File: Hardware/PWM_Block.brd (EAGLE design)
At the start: 30.5 x 53.3 mm, 51 parts, among them U1 PCA9685, U2 PCA9306, U3 EDISON_CONNECTOR_FULLMOUNTING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, U4 EDISON_CONNECTOR_FULLHEADER

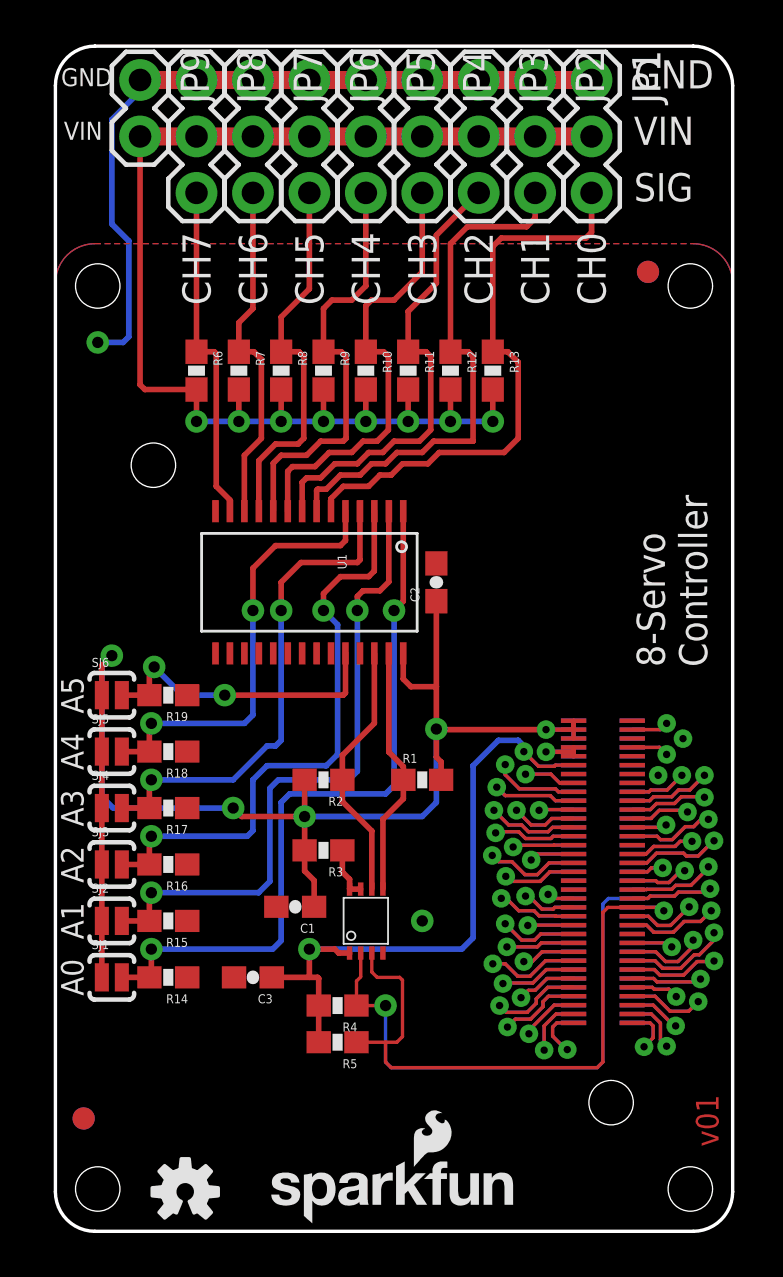
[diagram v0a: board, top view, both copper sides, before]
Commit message: Added DCIN pin Corrected Header footprint Renamed board and files Cleaned up dimensions and added units Added VSYS -> VIN circuit Added DNP to pullup resistors
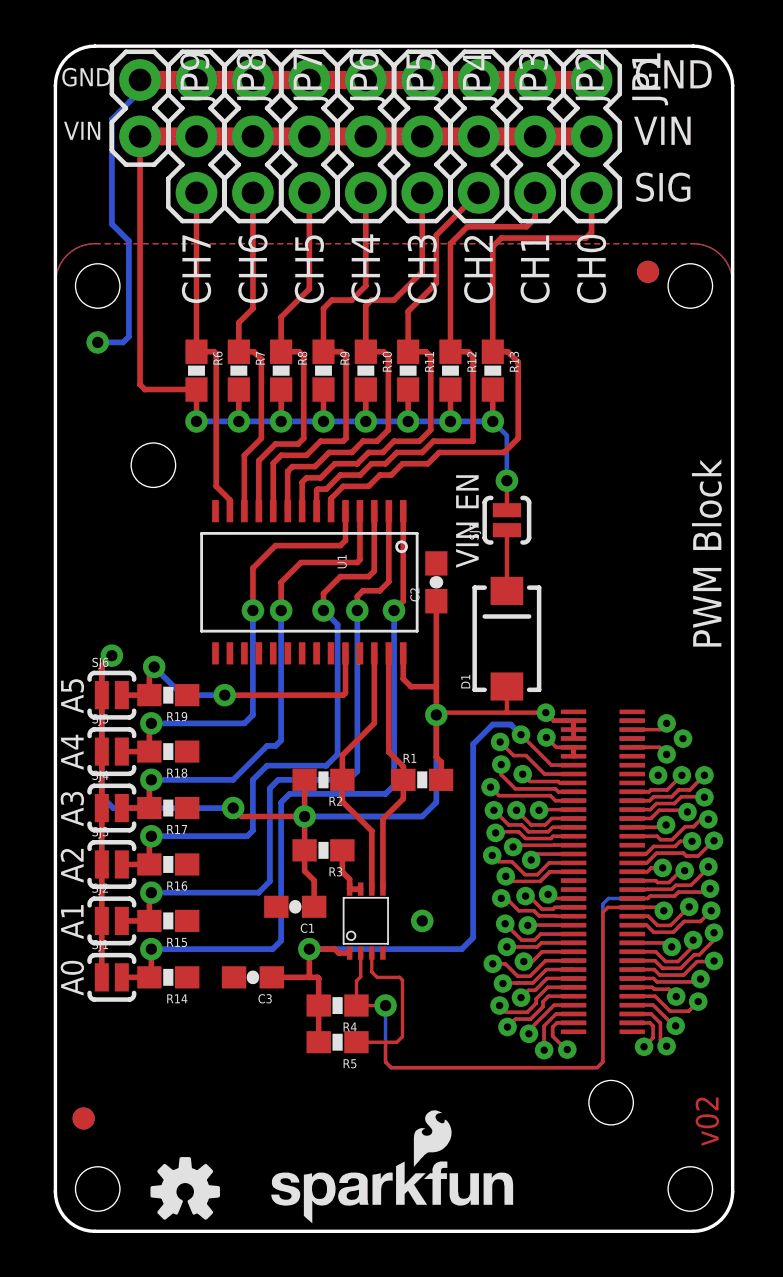
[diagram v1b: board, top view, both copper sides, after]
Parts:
- added D1: B340A, SparkFun-DiscreteSemi:SMA-DIODE
- added SJ7: VIN_ENABLE, SparkFun-Passives:PAD-JUMPER-2-NO_YES_SILK
- R4, R5: value 2.2k -> DNP
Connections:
- new net DCIN: U3.14, U4.14
- new net N$2: D1.C, SJ7.1
- net VCC: now also SJ7.2
- net VSYS: now also D1.A
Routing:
- net DCIN: track 0.00 -> 7.80 mm, vias 0 -> 1
- net VCC: track 58.9 -> 63.2 mm, vias 8 -> 9
- net N$2: track 0.00 -> 2.73 mm
- net VSYS: track 67.1 -> 69.3 mm
- net 1.8V: track 31.7 -> 33.0 mm
- net USB_VBUS: track 7.42 -> 7.98 mm
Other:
- board text added: "NOTE: Units are in Inches"
- board text added: "PWM Block"
- board text added: "VIN EN"
- board text added: "v02"
- board text removed: "8-Servo Controller"
- board text removed: "Connectors Go Here"
- board text removed: "LED's and selector switches go here"
- board text removed: "Nothing goes here... I mean it."
- board text removed: "v01"

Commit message: Rev to 10. Fix gnd and pwr, text
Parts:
- R1, R2: value 2.2k -> 10K
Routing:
- net VSYS: track 69.3 -> 72.1 mm
- net 3.3V: track 4.01 -> 6.47 mm
- net USB_VBUS: track 7.98 -> 8.99 mm
- net USB_DP: track 4.90 -> 5.92 mm
- net USB_DN: track 8.06 -> 9.08 mm
- net DCIN: track 7.80 -> 8.82 mm
- net 1.8V: track 33.0 -> 33.6 mm
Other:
- board text added: "v10"
- board text removed: "v02"

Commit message: Touch up packages, silk for reds
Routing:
- net N$1: track 2.38 -> 3.60 mm
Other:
- board text added: "VSYS->VIN"
- board text removed: "VIN EN"
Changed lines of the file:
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@@
 <layer number="2" name="Route2" color="1" fill="3" visible="no" active="yes"/>
 <layer number="15" name="Route15" color="4" fill="6" visible="no" active="yes"/>
-<layer number="16" name="Bottom" color="1" fill="1" visible="no" active="yes"/>
+<layer number="16" name="Bottom" color="1" fill="1" visible="yes" active="yes"/>
 <layer number="17" name="Pads" color="2" fill="1" visible="yes" active="yes"/>
 <layer number="18" name="Vias" color="2" fill="1" visible="yes" active="yes"/>
@@
 <layer number="20" name="Dimension" color="15" fill="1" visible="yes" active="yes"/>
 <layer number="21" name="tPlace" color="16" fill="1" visible="yes" active="yes"/>
-<layer number="22" name="bPlace" color="14" fill="1" visible="no" active="yes"/>
+<layer number="22" name="bPlace" color="14" fill="1" visible="yes" active="yes"/>
 <layer number="23" name="tOrigins" color="15" fill="1" visible="yes" active="yes"/>
-<layer number="24" name="bOrigins" color="15" fill="1" visible="no" active="yes"/>
+<layer number="24" name="bOrigins" color="15" fill="1" visible="yes" active="yes"/>
 <layer number="25" name="tNames" color="7" fill="1" visible="no" active="yes"/>
 <layer number="26" name="bNames" color="7" fill="1" visible="no" active="yes"/>
@@
 <layer number="43" name="vRestrict" color="2" fill="10" visible="no" active="yes"/>
 <layer number="44" name="Drills" color="7" fill="1" visible="no" active="yes"/>
-<layer number="45" name="Holes" color="7" fill="1" visible="no" active="yes"/>
+<layer number="45" name="Holes" color="7" fill="1" visible="yes" active="yes"/>
 <layer number="46" name="Milling" color="3" fill="1" visible="no" active="yes"/>
-<layer number="51" name="tDocu" color="6" fill="1" visible="no" active="yes"/>
+<layer number="51" name="tDocu" color="6" fill="1" visible="yes" active="yes"/>
 <layer number="3" name="Route3" color="4" fill="3" visible="no" active="no"/>
 <layer number="4" name="Route4" color="1" fill="4" visible="no" active="no"/>
@@
 <text x="29.21" y="6.35" size="1.016" layer="22" font="vector" ratio="15" rot="SMR270" align="center">4xM2.0</text>
 <text x="29.845" y="3.81" size="1.016" layer="1" font="vector" ratio="15" rot="R90">v10</text>
-<text x="29.21" y="52.07" size="1.27" layer="22" font="vector" ratio="15" rot="MR0" align="center-left">GND</text>
-<text x="29.21" y="49.53" size="1.27" layer="22" font="vector" ratio="15" rot="MR0" align="center-left">VIN</text>
-<text x="29.21" y="46.99" size="1.27" layer="22" font="vector" ratio="15" rot="MR0" align="center-left">SIG</text>
-<text x="26.035" y="52.07" size="1.27" layer="21" font="vector" ratio="15" align="center-left">GND</text>
-<text x="26.035" y="49.53" size="1.27" layer="21" font="vector" ratio="15" align="center-left">VIN</text>
-<text x="26.035" y="46.99" size="1.27" layer="21" font="vector" ratio="15" align="center-left">SIG</text>
+<text x="25.908" y="52.07" size="1.27" layer="22" font="vector" ratio="15" rot="SMR180" align="center-left">GND</text>
+<text x="26.035" y="49.53" size="1.27" layer="22" font="vector" ratio="15" rot="SMR180" align="center-left">VIN</text>
+<text x="25.908" y="46.99" size="1.27" layer="22" font="vector" ratio="15" rot="SMR180" align="center-left">SIG</text>
+<text x="28.956" y="51.943" size="1.27" layer="21" font="vector" ratio="15" rot="SR180" align="center-left">GND</text>
+<text x="28.575" y="49.53" size="1.27" layer="21" font="vector" ratio="15" rot="SR180" align="center-left">VIN</text>
+<text x="28.575" y="46.99" size="1.27" layer="21" font="vector" ratio="15" rot="SR180" align="center-left">SIG</text>
 <text x="29.972" y="26.162" size="1.27" layer="21" font="vector" ratio="15" rot="R90">PWM Block</text>
-<text x="0.254" y="51.943" size="0.8128" layer="21" font="vector" ratio="15" align="center-left">GND</text>
-<text x="0.381" y="49.53" size="0.8128" layer="21" font="vector" ratio="15" align="center-left">VIN</text>
-<text x="2.159" y="49.53" size="0.8128" layer="22" font="vector" ratio="15" rot="MR0" align="center-left">VIN</text>
-<text x="2.286" y="51.943" size="0.8128" layer="22" font="vector" ratio="15" rot="MR0" align="center-left">GND</text>
+<text x="2.286" y="51.816" size="0.8128" layer="21" font="vector" ratio="15" rot="SR180" align="center-left">GND</text>
+<text x="2.286" y="49.53" size="0.8128" layer="21" font="vector" ratio="15" rot="SR180" align="center-left">VIN</text>
+<text x="0.508" y="49.53" size="0.8128" layer="22" font="vector" ratio="15" rot="SMR180" align="center-left">VIN</text>
+<text x="0.635" y="51.689" size="0.8128" layer="22" font="vector" ratio="15" rot="SMR180" align="center-left">GND</text>
 <text x="24.13" y="44.958" size="1.27" layer="21" font="vector" ratio="15" rot="R270" align="center-left">CH0</text>
 <text x="21.59" y="44.958" size="1.27" layer="21" font="vector" ratio="15" rot="R270" align="center-left">CH1</text>
@@
 <text x="31.75" y="-2.54" size="1.778" layer="51">NOTE: Units are in Inches</text>
 <text x="29.972" y="35.814" size="1.27" layer="22" font="vector" ratio="15" rot="SMR270">PWM Block</text>
-<text x="24.257" y="32.004" size="1.016" layer="21" font="vector" ratio="15" align="center">VIN EN</text>
+<text x="22.606" y="32.131" size="1.016" layer="21" font="vector" ratio="15" rot="R90" align="center">VSYS-&gt;VIN</text>
 </plain>
 <attributes>
@@
 <contactref element="U2" pad="8"/>
 <contactref element="U2" pad="7"/>
-<wire x1="13.24" y1="15.4008" x2="13.74" y2="15.4008" width="0.254" layer="1"/>
 <wire x1="13.24" y1="15.4008" x2="13.24" y2="15.843" width="0.254" layer="1"/>
 <wire x1="13.24" y1="15.843" x2="12.915" y2="16.168" width="0.254" layer="1"/>
-<wire x1="12.915" y1="17.145" x2="12.915" y2="16.168" width="0.254" layer="1"/>
+<wire x1="12.915" y1="17.145" x2="12.915" y2="16.383" width="0.254" layer="1"/>
+<wire x1="12.915" y1="16.383" x2="12.915" y2="16.168" width="0.254" layer="1"/>
+<wire x1="13.74" y1="15.4008" x2="13.74" y2="16.232" width="0.1524" layer="1"/>
+<wire x1="13.74" y1="16.232" x2="13.589" y2="16.383" width="0.1524" layer="1"/>
+<wire x1="13.589" y1="16.383" x2="12.915" y2="16.383" width="0.1524" layer="1"/>
 </signal>
 <signal name="HV_SCL">

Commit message: Ready for reds Thicken VSYS->VIN trace Fix a stray ground thermal on PCA9306 No known to-do items
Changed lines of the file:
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@@
 <text x="29.972" y="35.814" size="1.27" layer="22" font="vector" ratio="15" rot="SMR270">PWM Block</text>
 <text x="22.606" y="32.131" size="1.016" layer="21" font="vector" ratio="15" rot="R90" align="center">VSYS-&gt;VIN</text>
+<wire x1="14.986" y1="12.7" x2="14.986" y2="12.319" width="0.1524" layer="41"/>
 </plain>
 <attributes>
@@
 <wire x1="19.05" y1="49.276" x2="21.59" y2="49.276" width="0.8128" layer="1"/>
 <wire x1="21.59" y1="49.276" x2="24.13" y2="49.276" width="0.8128" layer="1"/>
-<wire x1="6.35" y1="37.885" x2="4.025" y2="37.885" width="0.254" layer="1"/>
-<wire x1="4.025" y1="37.885" x2="3.81" y2="38.1" width="0.254" layer="1"/>
-<wire x1="3.81" y1="38.1" x2="3.81" y2="49.276" width="0.254" layer="1"/>
+<wire x1="6.35" y1="37.885" x2="4.025" y2="37.885" width="0.5588" layer="1"/>
+<wire x1="4.025" y1="37.885" x2="3.81" y2="38.1" width="0.5588" layer="1"/>
+<wire x1="3.81" y1="38.1" x2="3.81" y2="49.276" width="0.5588" layer="1"/>
 <wire x1="8.255" y1="37.885" x2="8.255" y2="36.449" width="0.254" layer="1"/>
 <via x="8.255" y="36.449" extent="1-16" drill="0.508"/>
@@
 <wire x1="19.685" y1="37.885" x2="19.685" y2="36.449" width="0.254" layer="1"/>
 <via x="19.685" y="36.449" extent="1-16" drill="0.508"/>
-<wire x1="19.685" y1="36.449" x2="17.78" y2="36.449" width="0.254" layer="16"/>
-<wire x1="15.875" y1="36.449" x2="13.97" y2="36.449" width="0.254" layer="16"/>
-<wire x1="13.97" y1="36.449" x2="12.065" y2="36.449" width="0.254" layer="16"/>
-<wire x1="12.065" y1="36.449" x2="10.16" y2="36.449" width="0.254" layer="16"/>
-<wire x1="10.16" y1="36.449" x2="8.255" y2="36.449" width="0.254" layer="16"/>
-<wire x1="6.35" y1="37.885" x2="6.35" y2="36.449" width="0.254" layer="1"/>
+<wire x1="19.685" y1="36.449" x2="17.78" y2="36.449" width="0.5588" layer="16"/>
+<wire x1="15.875" y1="36.449" x2="13.97" y2="36.449" width="0.5588" layer="16"/>
+<wire x1="13.97" y1="36.449" x2="12.065" y2="36.449" width="0.5588" layer="16"/>
+<wire x1="12.065" y1="36.449" x2="10.16" y2="36.449" width="0.5588" layer="16"/>
+<wire x1="10.16" y1="36.449" x2="8.255" y2="36.449" width="0.5588" layer="16"/>
+<wire x1="6.35" y1="37.885" x2="6.35" y2="36.449" width="0.5588" layer="1"/>
 <via x="6.35" y="36.449" extent="1-16" drill="0.508"/>
-<wire x1="6.35" y1="36.449" x2="8.255" y2="36.449" width="0.254" layer="16"/>
-<wire x1="15.875" y1="36.449" x2="17.78" y2="36.449" width="0.254" layer="16"/>
+<wire x1="6.35" y1="36.449" x2="8.255" y2="36.449" width="0.5588" layer="16"/>
+<wire x1="15.875" y1="36.449" x2="17.78" y2="36.449" width="0.5588" layer="16"/>
 <contactref element="SJ7" pad="2"/>
-<wire x1="20.32" y1="32.454" x2="20.32" y2="33.782" width="0.2032" layer="1"/>
+<wire x1="20.32" y1="32.454" x2="20.32" y2="33.782" width="0.5588" layer="1"/>
 <via x="20.32" y="33.782" extent="1-16" drill="0.508"/>
-<wire x1="20.32" y1="33.782" x2="20.32" y2="35.814" width="0.2032" layer="16"/>
-<wire x1="20.32" y1="35.814" x2="19.685" y2="36.449" width="0.2032" layer="16"/>
+<wire x1="20.32" y1="33.782" x2="20.32" y2="35.814" width="0.5588" layer="16"/>
+<wire x1="20.32" y1="35.814" x2="19.685" y2="36.449" width="0.5588" layer="16"/>
 </signal>
 <signal name="A4">
@@
 <contactref element="D1" pad="C"/>
 <contactref element="SJ7" pad="1"/>
-<wire x1="20.32" y1="28.82" x2="20.32" y2="31.554" width="0.2032" layer="1"/>
+<wire x1="20.32" y1="28.82" x2="20.32" y2="31.554" width="0.5588" layer="1"/>
 </signal>
 </signals>
